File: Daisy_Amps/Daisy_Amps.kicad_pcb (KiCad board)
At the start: 2 copper layers, 13 parts, among them U1 MCP6004, U2 MCP6004, U3 MCP6004, U5 Daisy_Seed

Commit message: schematic done
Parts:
- removed U3: MCP6004, Package_SO:SOIC-14_3.9x8.7mm_P1.27mm
- added Audio_in_jack1: ACJS-MHOM, audiojack:CONN06_JACK_ACJS_15P75X25_AMP, F.Cu at (92.3, 57.0)
- added Audio_in_jack2: ACJS-MHOM, audiojack:CONN06_JACK_ACJS_15P75X25_AMP, F.Cu at (233.7, 68.0)
- added C10: 2.2NF, Capacitor_SMD:C_0805_2012Metric, F.Cu at (116.8, 113.9)
- added C11: 100NF, Capacitor_SMD:C_0805_2012Metric_Pad1.18x1.45mm_HandSolder, F.Cu at (112.1, 105.3)
- added C12: 100NF, Capacitor_SMD:C_0805_2012Metric_Pad1.18x1.45mm_HandSolder, F.Cu at (112.1, 108.3)
- added C3: 10UF, Capacitor_SMD:C_0805_2012Metric_Pad1.18x1.45mm_HandSolder, F.Cu at (112.1, 93.2)
- added C4: 10UF, Capacitor_SMD:C_0805_2012Metric_Pad1.18x1.45mm_HandSolder, F.Cu at (112.1, 96.2)
- added C5: 100NF, Capacitor_SMD:C_0805_2012Metric, F.Cu at (150.6, 93.2)
- added C6: 100NF, Capacitor_SMD:C_0805_2012Metric, F.Cu at (150.6, 96.2)
- added C7: 10UF, Capacitor_SMD:C_0805_2012Metric_Pad1.18x1.45mm_HandSolder, F.Cu at (112.1, 99.2)
- added C8: 10UF, Capacitor_SMD:C_0805_2012Metric_Pad1.18x1.45mm_HandSolder, F.Cu at (112.1, 102.3)
- added C9: 2.2NF, Capacitor_SMD:C_0805_2012Metric, F.Cu at (116.8, 110.9)
- added J1: Power and Ground, Connector_PinSocket_2.54mm:PinSocket_1x02_P2.54mm_Vertical, F.Cu at (96.0, 108.5)
- added R1: 2M, Resistor_SMD:R_0805_2012Metric_Pad1.20x1.40mm_HandSolder, F.Cu at (146.0, 93.2)
- added R10: 100R, Resistor_THT:R_Axial_DIN0207_L6.3mm_D2.5mm_P7.62mm_Horizontal, F.Cu at (120.8, 105.5)
- added R11: 2M, Resistor_SMD:R_0805_2012Metric_Pad1.20x1.40mm_HandSolder, F.Cu at (116.9, 102.0)
- added R12: 100R, Resistor_THT:R_Axial_DIN0207_L6.3mm_D2.5mm_P7.62mm_Horizontal, F.Cu at (120.8, 109.5)
- added R13: 2M, Resistor_SMD:R_0805_2012Metric_Pad1.20x1.40mm_HandSolder, F.Cu at (116.9, 105.0)
- added R14: 3.3K, Resistor_SMD:R_0805_2012Metric, F.Cu at (111.9, 111.3)
- added R15: 3.3K, Resistor_SMD:R_0805_2012Metric, F.Cu at (111.9, 114.2)
- added R16: 2M, Resistor_SMD:R_0805_2012Metric_Pad1.20x1.40mm_HandSolder, F.Cu at (116.9, 108.0)
- added R2: 2M, Resistor_SMD:R_0805_2012Metric_Pad1.20x1.40mm_HandSolder, F.Cu at (146.0, 96.2)
- added R3: 2M, Resistor_SMD:R_0805_2012Metric_Pad1.20x1.40mm_HandSolder, F.Cu at (146.0, 99.1)
- added R4: 2M, Resistor_SMD:R_0805_2012Metric_Pad1.20x1.40mm_HandSolder, F.Cu at (146.0, 102.0)
- added R5: 2M, Resistor_SMD:R_0805_2012Metric_Pad1.20x1.40mm_HandSolder, F.Cu at (146.0, 105.0)
- added R7: 2M, Resistor_SMD:R_0805_2012Metric_Pad1.20x1.40mm_HandSolder, F.Cu at (116.9, 93.2)
- added R8: 2M, Resistor_SMD:R_0805_2012Metric_Pad1.20x1.40mm_HandSolder, F.Cu at (116.9, 96.2)
- added R9: 2M, Resistor_SMD:R_0805_2012Metric_Pad1.20x1.40mm_HandSolder, F.Cu at (116.9, 99.1)
- I2C_Output_Pins1: footprint Connector_PinSocket_1.27mm:PinSocket_1x02_P1.27mm_Vertical -> Connector_PinHeader_2.54mm:PinHeader_1x02_P2.54mm_Vertical
- R6: footprint Resistor_SMD:R_0805_2012Metric -> Resistor_SMD:R_0805_2012Metric_Pad1.20x1.40mm_HandSolder
- U1: footprint Package_SO:SOIC-14_3.9x8.7mm_P1.27mm -> Package_DIP:DIP-14_W7.62mm
- U2: value MCP6004 -> OPA2134; footprint Package_SO:SOIC-14_3.9x8.7mm_P1.27mm -> Package_DIP:DIP-8_W7.62mm_LongPads
- moved U5 116.9 mm to (170.4, 62.0)
- moved I2C_Output_Pins1 98.1 mm to (158.0, 90.7)
- moved U2 70.6 mm to (133.2, 101.9)
- moved U1 49.3 mm to (131.7, 64.9)
- moved C1 13.5 mm to (97.0, 39.5)
- moved R1 13.5 mm to (92.6, 29.1)
- moved R2 13.5 mm to (92.6, 32.0)
- moved R3 13.5 mm to (92.6, 35.0)
- moved R4 13.5 mm to (92.6, 38.0)
- moved R5 1.90 mm to (82.5, 47.5)
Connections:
- C1 pad 2: Net-(U3A-+) -> Net-(U1C-+)
- C2 pad 2: Net-(U2A-+) -> Net-(U1B-+)
- U1 pad 10: (no net) -> Net-(U1C-+)
- U1 pad 11: (no net) -> GND
- U1 pad 12: (no net) -> unconnected-(U1D-+-Pad12)
- U1 pad 13: (no net) -> unconnected-(U1D---Pad13)
- U1 pad 14: (no net) -> unconnected-(U1-Pad14)
- U1 pad 4: (no net) -> +5V
- U1 pad 5: (no net) -> Net-(U1B-+)
- U1 pad 6: (no net) -> /Input PreAmp/Audio_in_daisy_left
- U1 pad 7: (no net) -> /Input PreAmp/Audio_in_daisy_left
- U1 pad 8: (no net) -> /Input PreAmp/Audio_in_daisy_right
- U1 pad 9: (no net) -> /Input PreAmp/Audio_in_daisy_right
- U2 pad 1: /Input PreAmp/Audio_in_daisy_left -> Net-(U2A--)
- U2 pad 2: /Input PreAmp/Audio_in_daisy_left -> Net-(U2A--)
- U2 pad 4: (no net) -> GND
- U2 pad 5: (no net) -> Net-(U2B-+)
- U2 pad 6: (no net) -> Net-(U2B--)
- U2 pad 7: (no net) -> Net-(U2B--)
- U2 pad 8: (no net) -> +5V
- U5 pad 1: GND -> unconnected-(U5-D0-Pad1)
- U5 pad 10: GND -> unconnected-(U5-D9-Pad10)
- U5 pad 11: GND -> unconnected-(U5-D10-Pad11)
- U5 pad 2: GND -> unconnected-(U5-D1-Pad2)
- U5 pad 3: GND -> unconnected-(U5-D2-Pad3)
- U5 pad 4: GND -> unconnected-(U5-D3-Pad4)
- U5 pad 5: GND -> unconnected-(U5-D4-Pad5)
- U5 pad 6: GND -> unconnected-(U5-D5-Pad6)
- U5 pad 7: GND -> unconnected-(U5-D6-Pad7)
- U5 pad 8: GND -> unconnected-(U5-D7-Pad8)
- U5 pad 9: GND -> unconnected-(U5-D8-Pad9)
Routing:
- net /Output Amp/Audio_out_daisy_right: track 0.00 -> 15.9 mm
- net Net-(I2C_Output_Pins1-Pin_2): track 0.00 -> 12.6 mm
- net Net-(I2C_Output_Pins1-Pin_1): track 0.00 -> 12.6 mm

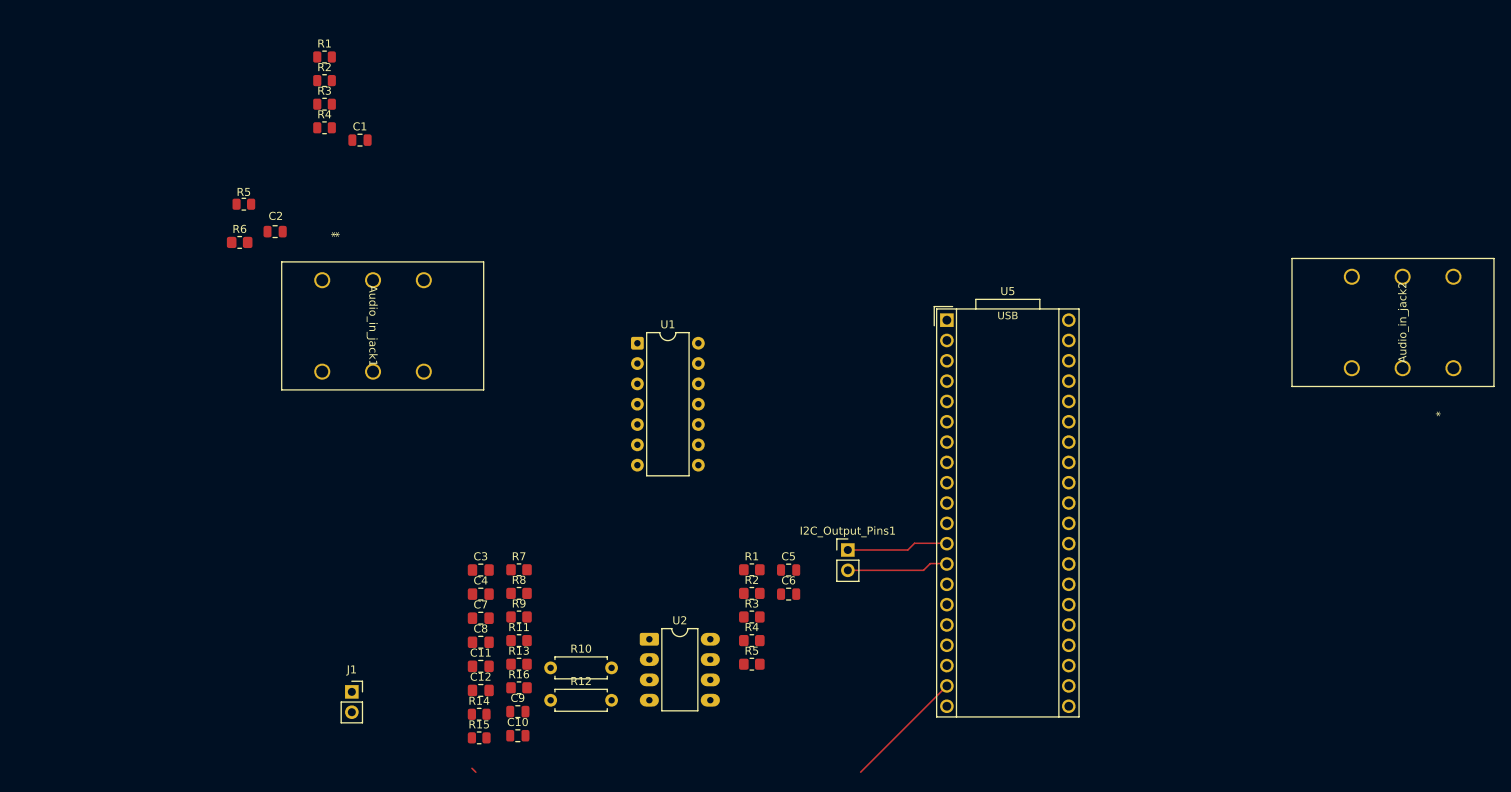
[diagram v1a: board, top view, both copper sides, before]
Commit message: updated amp pcb layout
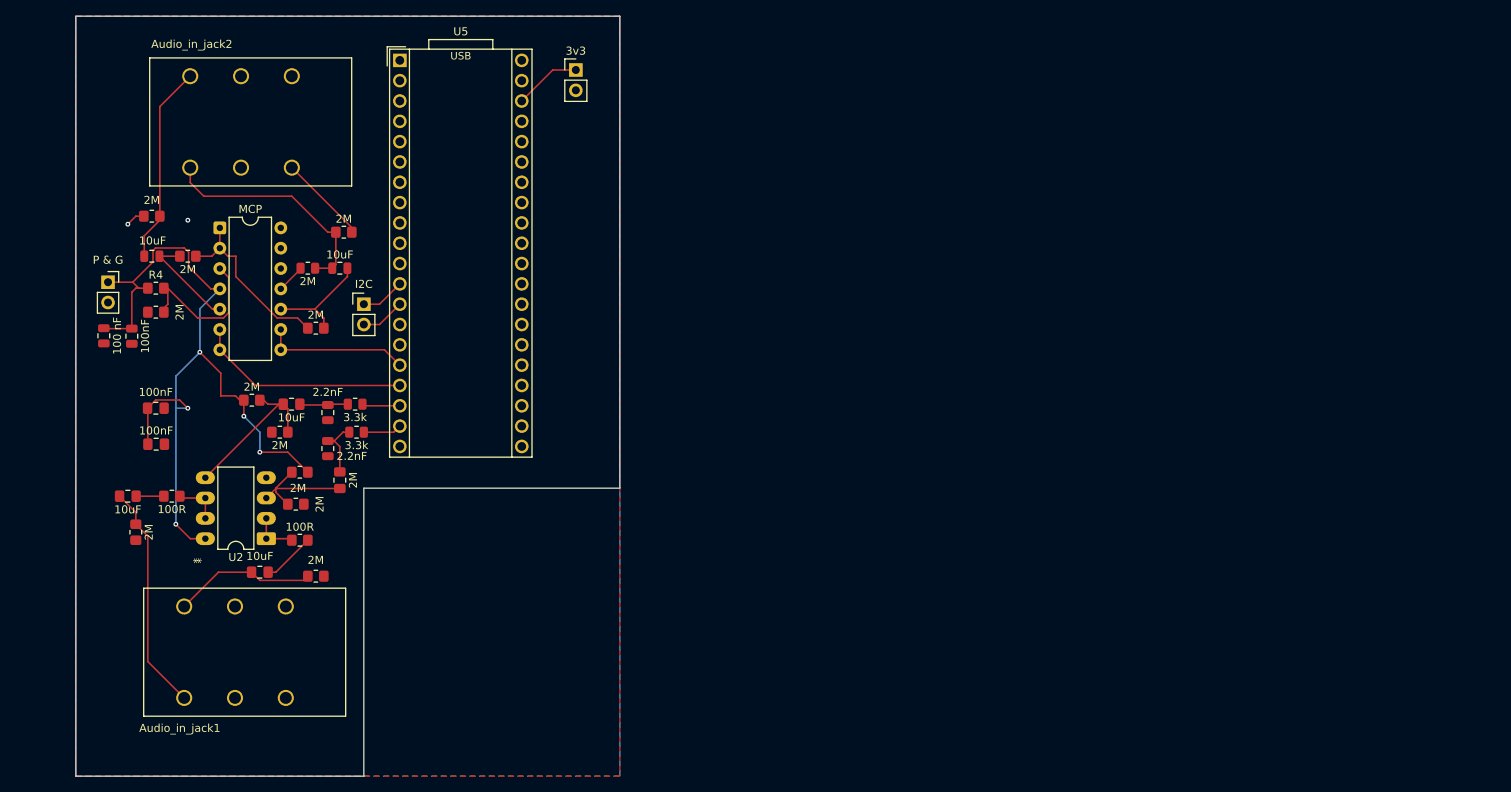
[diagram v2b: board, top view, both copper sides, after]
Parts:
- removed R2, R3: 2M, Resistor_SMD:R_0805_2012Metric
- removed the R4 at (92.6, 38.0)
- removed R5: 100K, Resistor_SMD:R_0805_2012Metric
- added 3v3: Conn_01x02_Pin, Connector_PinHeader_2.54mm:PinHeader_1x02_P2.54mm_Vertical, F.Cu at (124.0, 30.7)
- 100 nF: renamed from C5
- 100R: renamed from R10; footprint Resistor_THT:R_Axial_DIN0207_L6.3mm_D2.5mm_P7.62mm_Horizontal -> Resistor_SMD:R_0805_2012Metric_Pad1.20x1.40mm_HandSolder
- 100R: renamed from R12; footprint Resistor_THT:R_Axial_DIN0207_L6.3mm_D2.5mm_P7.62mm_Horizontal -> Resistor_SMD:R_0805_2012Metric_Pad1.20x1.40mm_HandSolder
- 10uF: renamed from C2; value 10UF -> 2M
- P & G: renamed from J1; value Power and Ground -> P & G
- moved Audio_in_jack2 162.1 mm to (75.8, 31.5), turned to -90 degrees
- moved 100 nF 90.5 mm to (65.0, 64.0), turned to -90 degrees
- moved 100nF 88.2 mm to (68.5, 64.0), turned to -90 degrees
- moved R4 86.5 mm to (71.5, 58.0)
- moved 2M 86.5 mm to (71.5, 61.0)
- moved 2M 83.7 mm to (75.5, 54.0), turned to 180 degrees
- moved U5 75.7 mm to (102.0, 29.5)
- moved I2C 67.9 mm to (97.5, 60.0)
- moved 2M 66.2 mm to (95.0, 51.0)
- moved 2M 63.8 mm to (91.5, 63.0)
- moved P & G 59.6 mm to (65.5, 57.2)
- moved MCP 54.2 mm to (79.5, 50.5)
- moved 100R 52.0 mm to (73.5, 84.0), turned to 180 degrees
- moved 100nF 51.9 mm to (71.5, 73.0)
- moved 100nF 50.9 mm to (71.5, 77.5)
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- renumbered C11 to 100nF, C6 to 100nF, C12 to 100nF, C1 to 10uF, C8 to 10uF, C7 to 10uF, C4 to 10uF, C10 to 2.2nF, C9 to 2.2nF, R13 to 2M, R1 to 2M, C3 to 2M, R16 to 2M, R7 to 2M, R3 to 2M, R8 to 2M, R5 to 2M, R11 to 2M, R9 to 2M, R6 to 2M, R2 to 2M, R15 to 3.3k, R14 to 3.3k, I2C_Output_Pins1 to I2C, U1 to MCP
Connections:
- U5 pad 38: unconnected-(U5-3V3_D-Pad38) -> Net-(J2-Pin_1)
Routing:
- net +5V: track 0.00 -> 103.6 mm, vias 0 -> 5
- net /R_audio: track 0.00 -> 29.5 mm
- net /Output Amp/Audio_out_jack_left: track 0.00 -> 28.6 mm
- net /Input PreAmp/Audio_in_daisy_left: track 0.00 -> 26.9 mm
- net /L_audio: track 0.00 -> 25.4 mm
- net /Input PreAmp/V_AUDIOBIAS: track 0.00 -> 22.6 mm
- net Net-(U2B-+): track 0.00 -> 19.9 mm
- net Net-(U1A-+): track 0.00 -> 18.6 mm
- net /Input PreAmp/Audio_in_daisy_right: track 0.00 -> 18.2 mm
- net /Output Amp/Audio_out_jack_right: track 0.00 -> 17.9 mm
- net GND: track 0.00 -> 17.2 mm, vias 0 -> 2
- net Net-(U2A-+): track 0.00 -> 15.2 mm
- net Net-(U1C-+): track 0.00 -> 13.9 mm
- net Net-(U1B-+): track 0.00 -> 12.8 mm
- net /Output Amp/Audio_out_daisy_right: track 15.9 -> 4.81 mm
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- added copper zone on B.Cu, net GND
- added copper zone on F.Cu, net GND
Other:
- board outline added: 68 x 95 mm
